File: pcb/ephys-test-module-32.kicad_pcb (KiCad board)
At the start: 2 copper layers, 100 x 60 mm, 16 parts, among them J2 BSE-040-01-F-D-A-TR, J3 BSE-040-01-F-D-A-TR, J4 M20-8760242, J5 A79026-001, U1 AT24C64D-SSHM-T

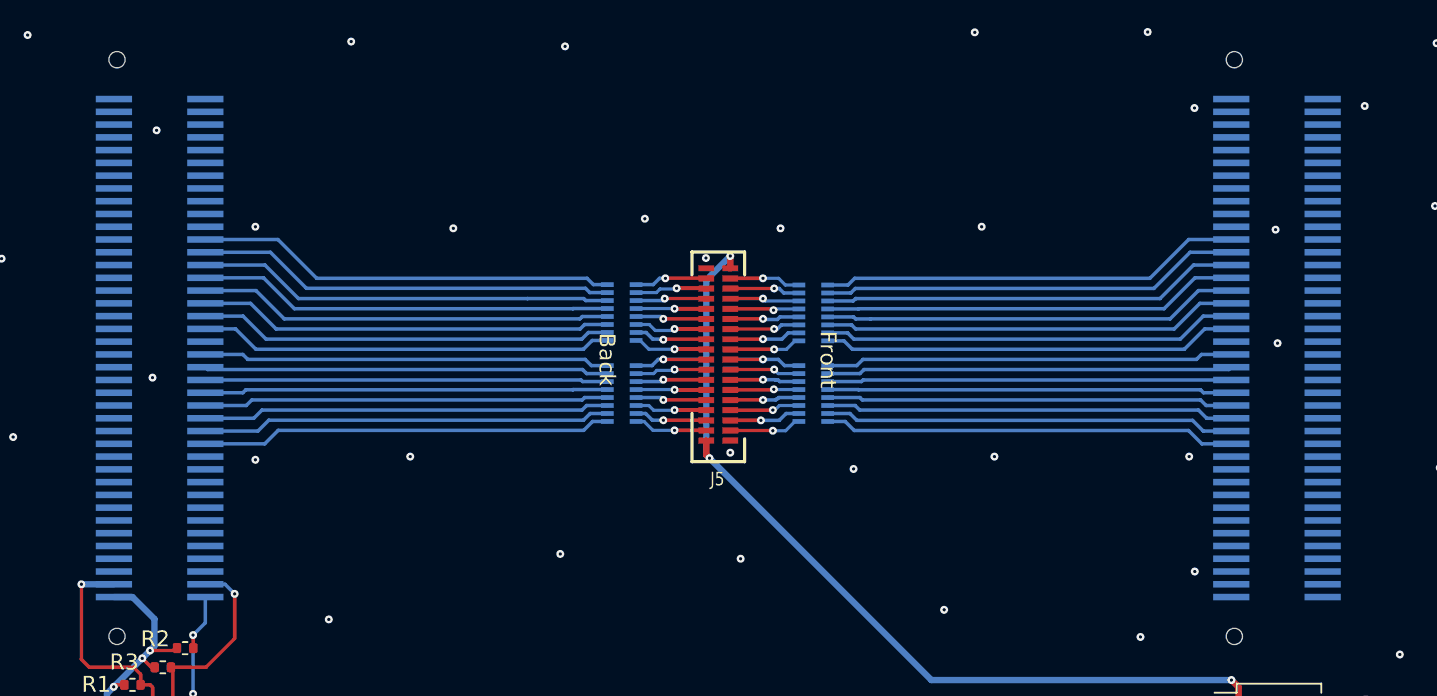
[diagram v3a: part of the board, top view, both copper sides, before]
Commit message: Libraries links updated
Removed local Libraries from Project
. KiCAD libraries
. open-ephys kicad library
. jonnew library

Created new manufacturing files
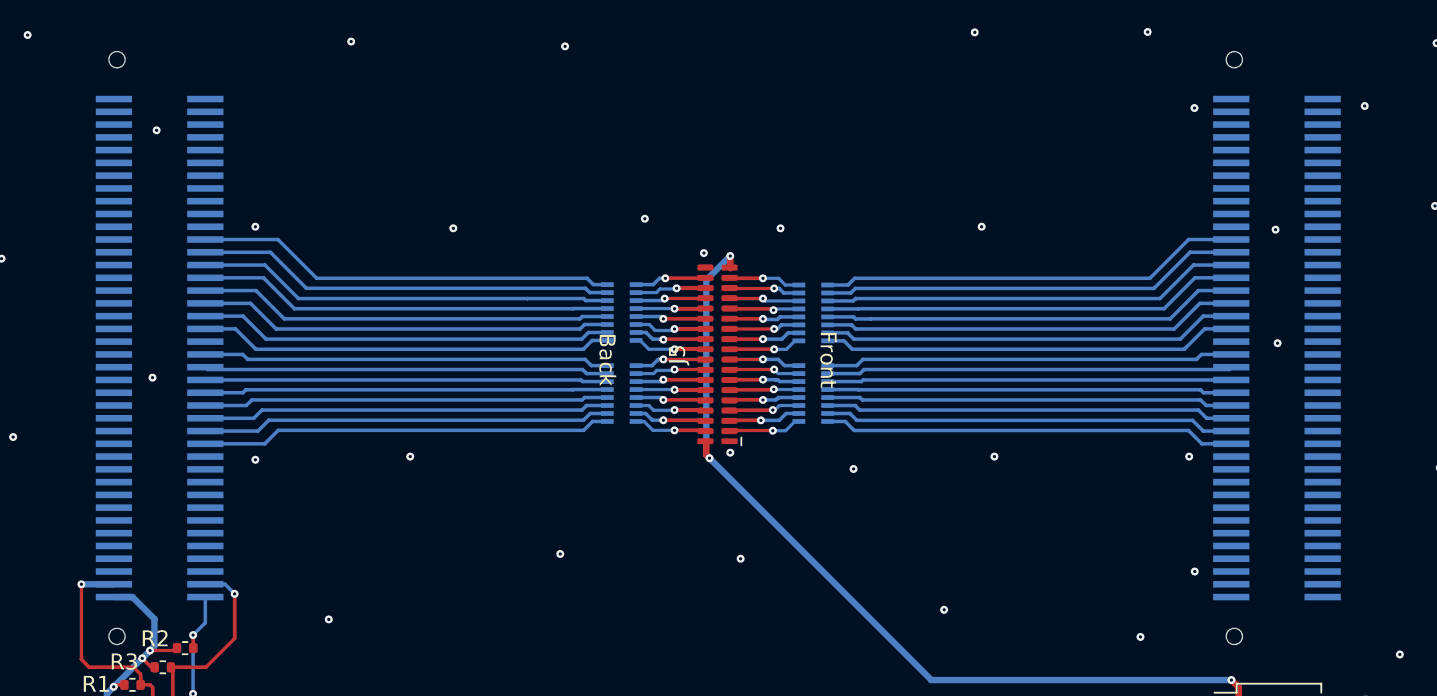
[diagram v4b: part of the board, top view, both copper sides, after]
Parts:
- H1: footprint _footprint Lib:OEPS_SN-STICKER-8x20mm -> open-ephys:OEPS_SN-STICKER-8x20mm
- J2, J3: footprint _footprint Lib:SAMTEC_BSE-040-01-X-D-A -> jonnew:SAMTEC_BSE-040-01-X-D-A
- J5: footprint _footprint Lib:A79026-001 -> jonnew:OMNETICS_A79026-001
- moved J5 0.32 mm to (157.9, 100.4), turned to 90 degrees
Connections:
- J5 pad 1: /Headstage Interface/REF -> GND
- J5 pad 10: /Headstage Interface/E23 -> /Headstage Interface/E22
- J5 pad 11: /Headstage Interface/E24 -> /Headstage Interface/E25
- J5 pad 12: /Headstage Interface/E25 -> /Headstage Interface/E24
- J5 pad 13: /Headstage Interface/E26 -> /Headstage Interface/E27
- J5 pad 14: /Headstage Interface/E27 -> /Headstage Interface/E26
- J5 pad 15: /Headstage Interface/E28 -> /Headstage Interface/E29
- J5 pad 16: /Headstage Interface/E29 -> /Headstage Interface/E28
- J5 pad 17: /Headstage Interface/E30 -> /Headstage Interface/E31
- J5 pad 18: /Headstage Interface/E31 -> /Headstage Interface/E30
- J5 pad 19: /Headstage Interface/E32 -> /Headstage Interface/E33
- J5 pad 2: GND -> /Headstage Interface/REF
- J5 pad 20: /Headstage Interface/E33 -> /Headstage Interface/E32
- J5 pad 21: /Headstage Interface/E34 -> /Headstage Interface/E35
- J5 pad 22: /Headstage Interface/E35 -> /Headstage Interface/E34
- J5 pad 23: /Headstage Interface/E36 -> /Headstage Interface/E37
- J5 pad 24: /Headstage Interface/E37 -> /Headstage Interface/E36
- J5 pad 25: /Headstage Interface/E38 -> /Headstage Interface/E39
- J5 pad 26: /Headstage Interface/E39 -> /Headstage Interface/E38
- J5 pad 27: /Headstage Interface/E40 -> /Headstage Interface/E41
- J5 pad 28: /Headstage Interface/E41 -> /Headstage Interface/E40
- J5 pad 29: /Headstage Interface/E42 -> /Headstage Interface/E43
- J5 pad 3: /Headstage Interface/E16 -> /Headstage Interface/E17
- J5 pad 30: /Headstage Interface/E43 -> /Headstage Interface/E42
- J5 pad 31: /Headstage Interface/E44 -> /Headstage Interface/E45
- J5 pad 32: /Headstage Interface/E45 -> /Headstage Interface/E44
- J5 pad 33: /Headstage Interface/E46 -> /Headstage Interface/E47
- J5 pad 34: /Headstage Interface/E47 -> /Headstage Interface/E46
- J5 pad 35: GND -> /Headstage Interface/REF
- J5 pad 36: /Headstage Interface/REF -> GND
- J5 pad 4: /Headstage Interface/E17 -> /Headstage Interface/E16
- J5 pad 5: /Headstage Interface/E18 -> /Headstage Interface/E19
- J5 pad 6: /Headstage Interface/E19 -> /Headstage Interface/E18
- J5 pad 7: /Headstage Interface/E20 -> /Headstage Interface/E21
- J5 pad 8: /Headstage Interface/E21 -> /Headstage Interface/E20
- J5 pad 9: /Headstage Interface/E22 -> /Headstage Interface/E23
